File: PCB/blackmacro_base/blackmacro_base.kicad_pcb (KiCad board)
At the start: 2 copper layers, 182.6 x 130.9 mm, 189 parts, among them J1 MOD Power, J2 MOD I/O, J3 Dial_PowerConn, J4 Dial_MagEncoderConn, J5 Dial_MotorControlConn, J6 USB_C_Receptacle_USB2.0_16P, Q1 AO3415, Q2 AO3415, Q3 AO3415, SW1 SW_SPDT, U1 HTP4056-42-ESOP8, U2 74HC238, U3 SN74LVC1T45DBV, U4 BQ27427, U5 MT3608L

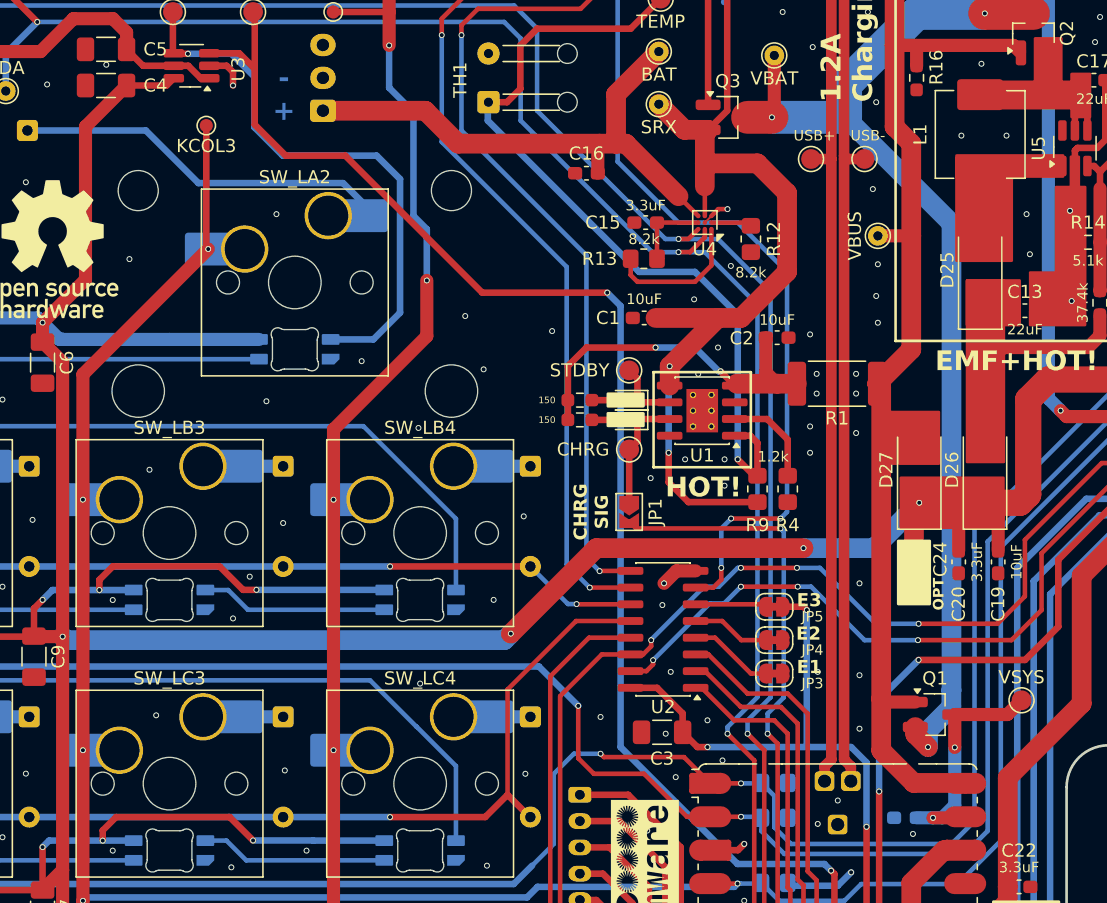
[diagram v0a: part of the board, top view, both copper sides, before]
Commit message: V2 pre-release BOM not done, updating gitignore to remove keebio-parts
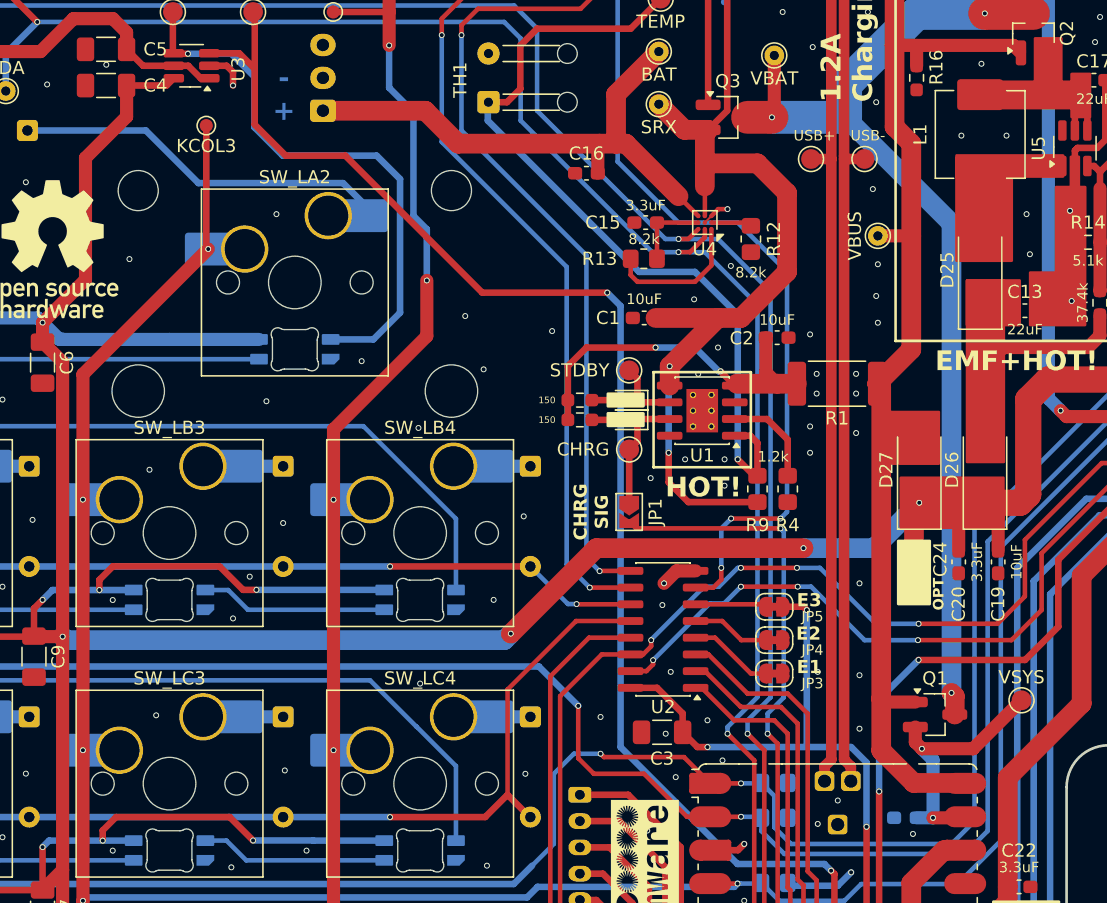
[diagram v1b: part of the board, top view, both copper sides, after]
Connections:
- Q1 pad 2: VBAT -> BAT_VSYS
- Q1 pad 3: BAT_VSYS -> VBAT
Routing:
- net VBAT: track 85.1 -> 80.1 mm
- net BAT_VSYS: track 18.5 -> 20.6 mm
